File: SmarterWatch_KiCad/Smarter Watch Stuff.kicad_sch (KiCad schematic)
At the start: 0 parts

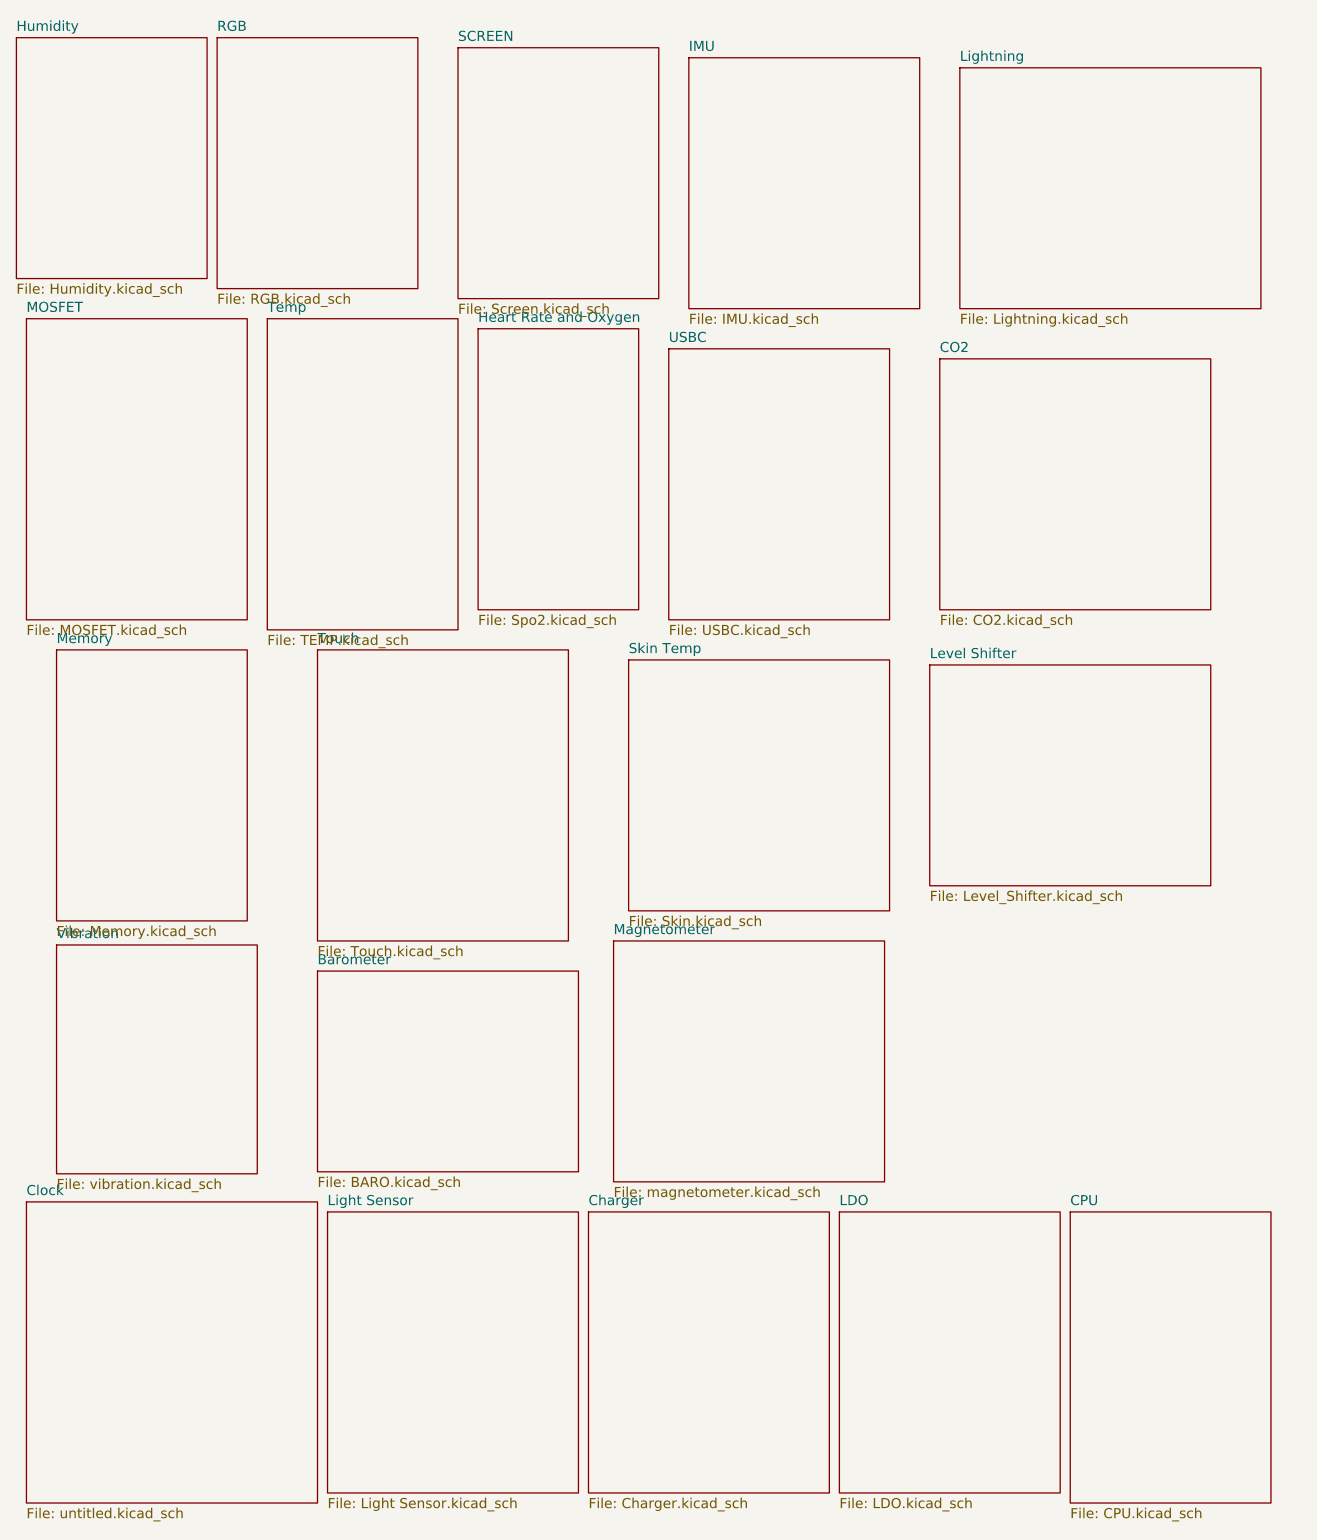
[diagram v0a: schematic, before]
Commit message: added pad to symbol
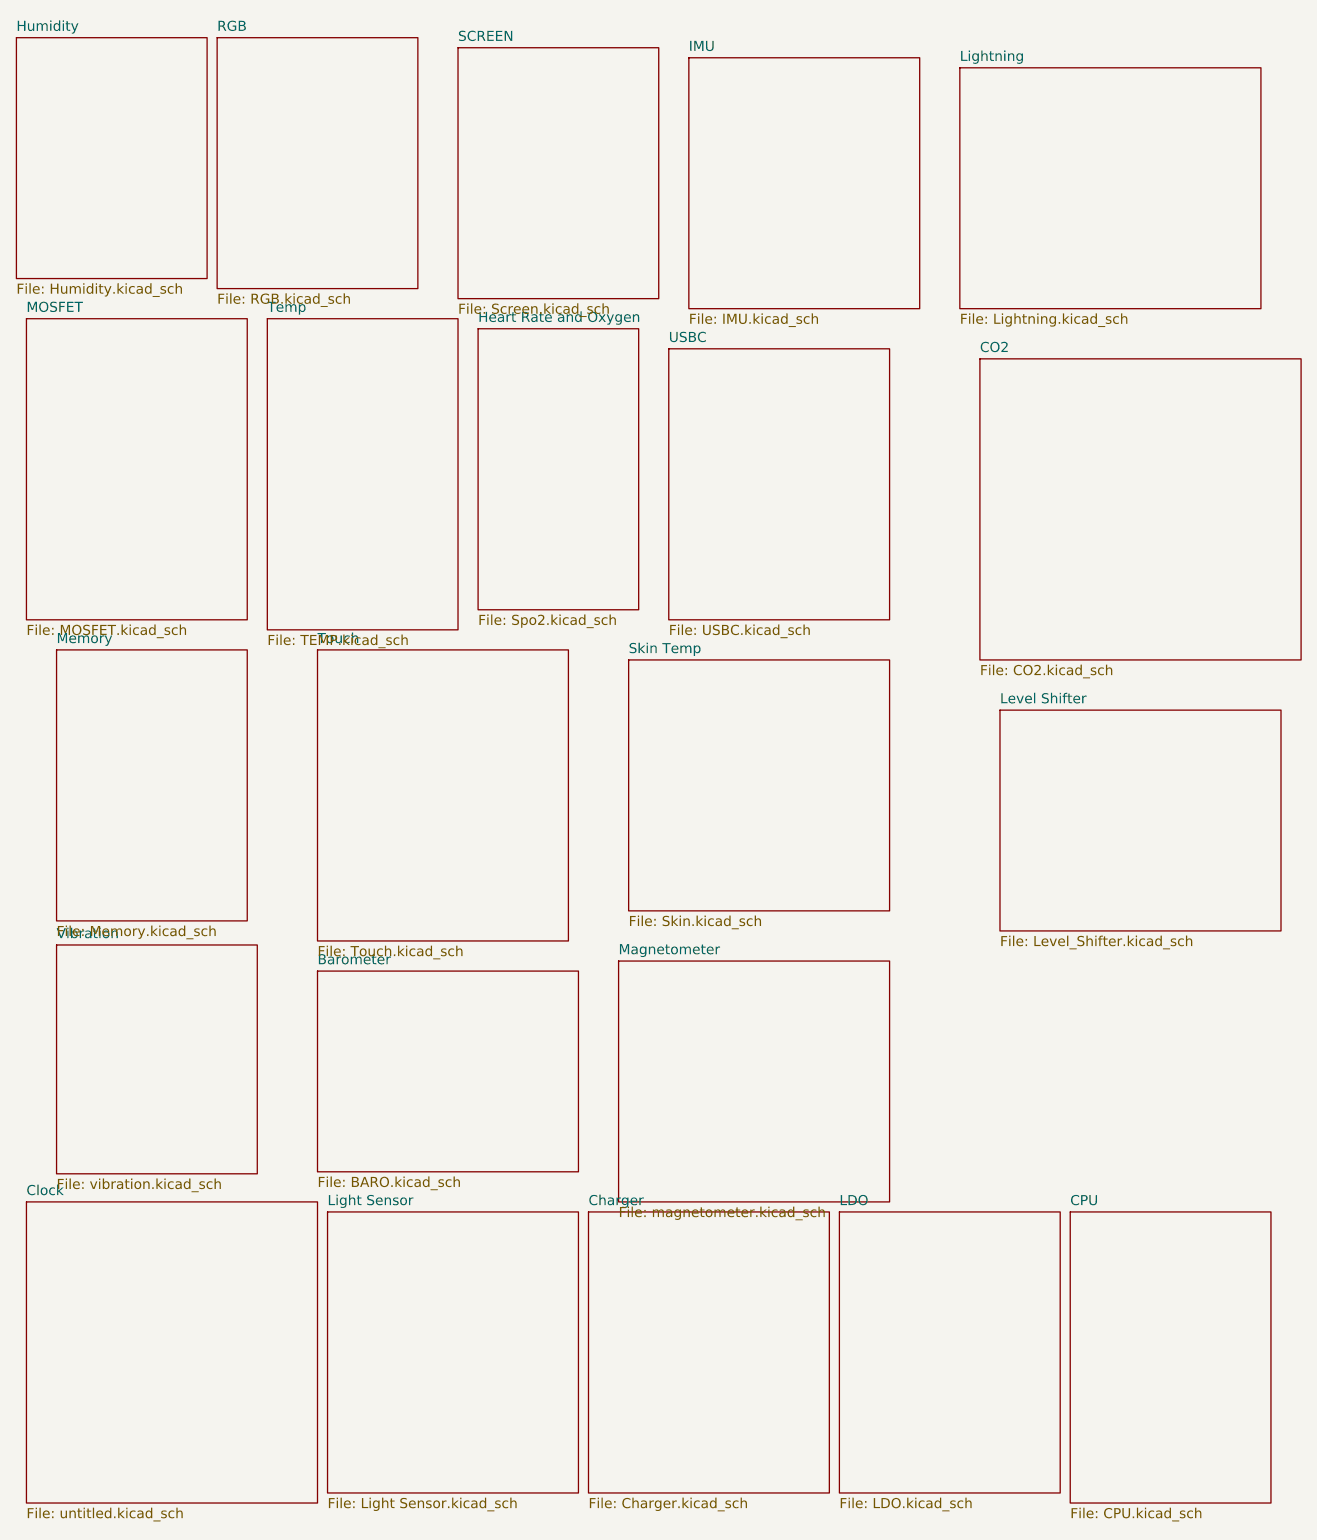
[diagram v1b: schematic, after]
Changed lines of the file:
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@@
 	)
 	(sheet
-		(at 129.54 53.34)
-		(size 34.29 31.75)
+		(at 134.62 53.34)
+		(size 40.64 38.1)
 		(exclude_from_sim no)
 		(in_bom yes)
@@
 		)
 		(property "Sheetname" "CO2"
-			(at 129.54 52.6284 0)
+			(at 134.62 52.6284 0)
 			(effects
 				(font
@@
 		)
 		(property "Sheetfile" "CO2.kicad_sch"
-			(at 129.54 85.6746 0)
+			(at 134.62 92.0246 0)
 			(effects
 				(font
@@
 	)
 	(sheet
-		(at 128.27 92.075)
+		(at 137.16 97.79)
 		(size 35.56 27.94)
 		(exclude_from_sim no)
@@
 		)
 		(property "Sheetname" "Level Shifter"
-			(at 128.27 91.3634 0)
+			(at 137.16 97.0784 0)
 			(effects
 				(font
@@
 		)
 		(property "Sheetfile" "Level_Shifter.kicad_sch"
-			(at 128.27 120.5996 0)
+			(at 137.16 126.3146 0)
 			(effects
 				(font
@@
 	)
 	(sheet
-		(at 88.265 127)
+		(at 88.9 129.54)
 		(size 34.29 30.48)
 		(exclude_from_sim no)
@@
 		)
 		(property "Sheetname" "Magnetometer"
-			(at 88.265 126.2884 0)
+			(at 88.9 128.8284 0)
 			(effects
 				(font
@@
 		)
 		(property "Sheetfile" "magnetometer.kicad_sch"
-			(at 88.265 158.0646 0)
-			(effects
-				(font
+			(at 88.9 160.6046 0)
+			(effects
+				(font
